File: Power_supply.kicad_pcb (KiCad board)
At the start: 2 copper layers, 116 x 60 mm, 44 parts, among them J1 Transformers, J2 240V, J20 HV_Transformer, J21 LV_Transformer, J22 220V, J23 Transformers, J25 Anodes_enable, J3 6V3, Q1 STP4NK60ZFP(MJE13003), Q10 MPSA42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

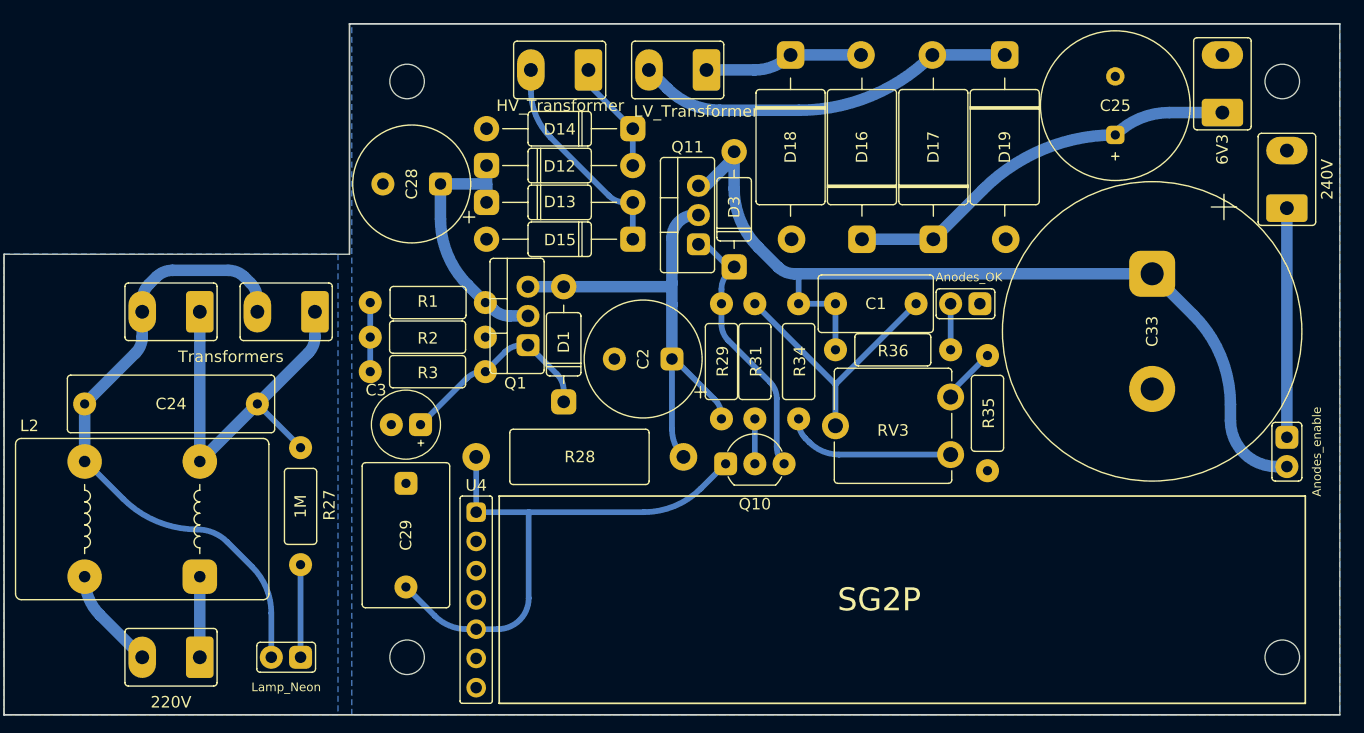
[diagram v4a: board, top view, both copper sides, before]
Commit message: Teardrops
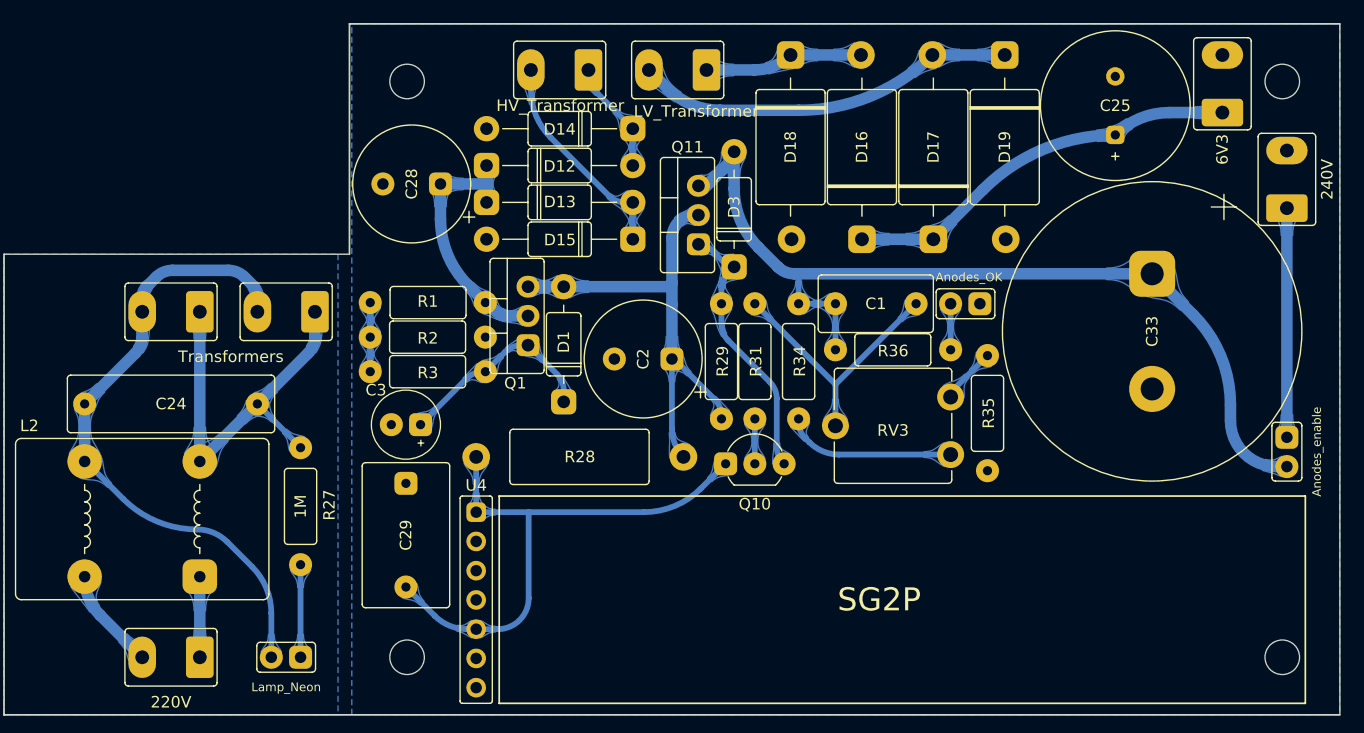
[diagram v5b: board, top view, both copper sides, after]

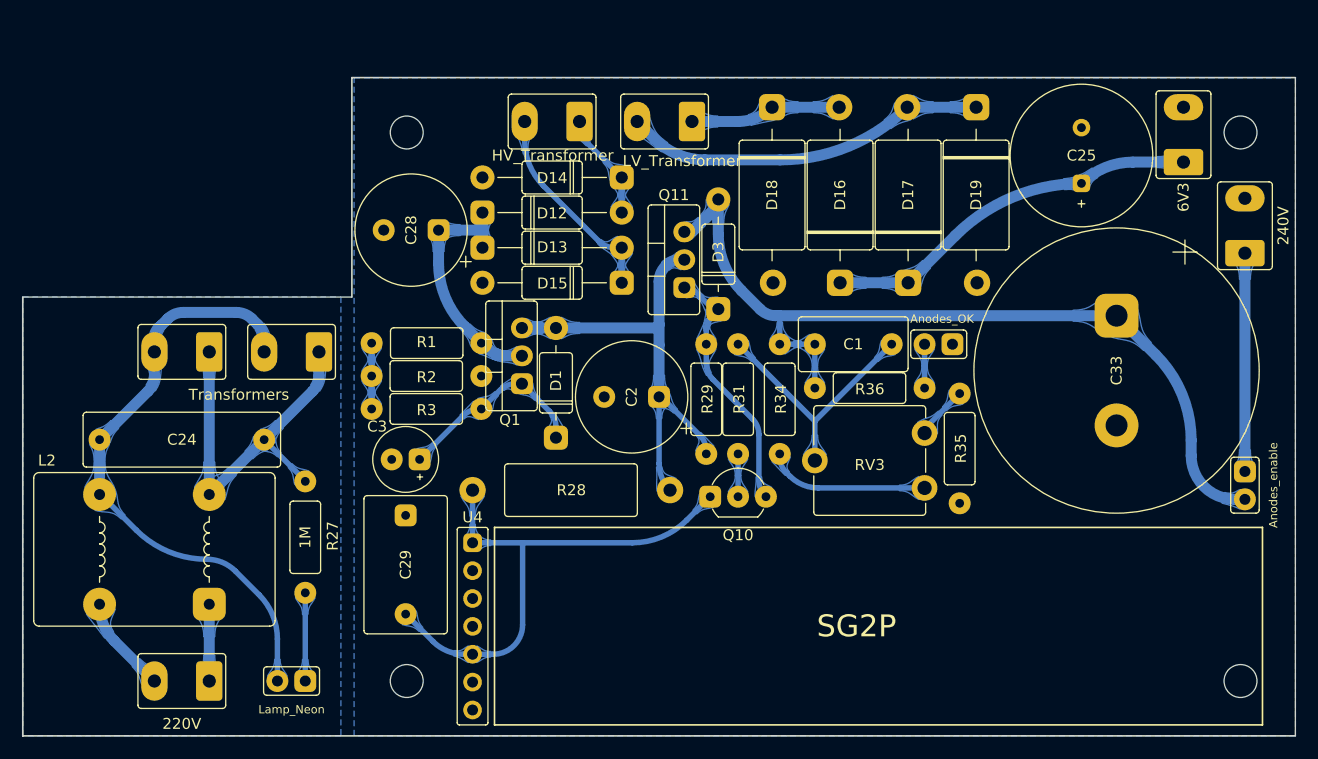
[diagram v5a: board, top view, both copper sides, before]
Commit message: Power supply PCB updated
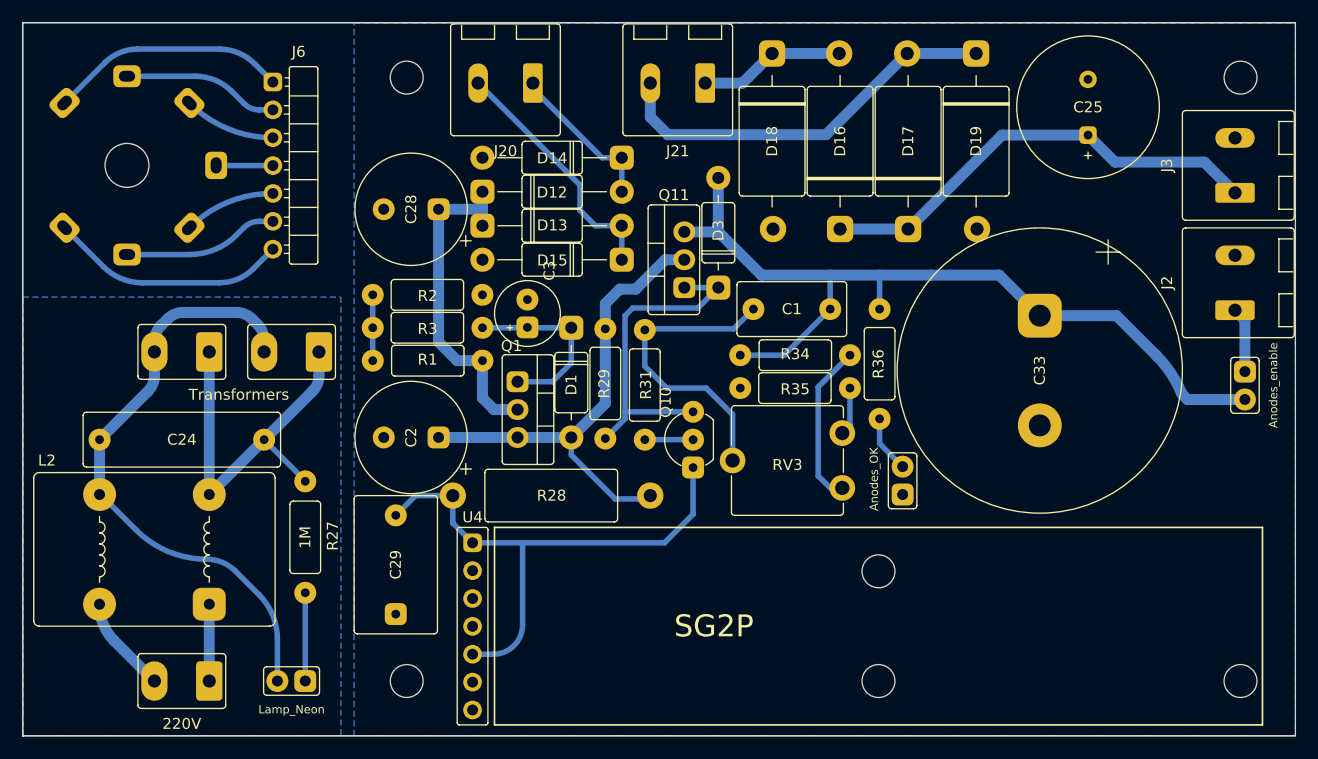
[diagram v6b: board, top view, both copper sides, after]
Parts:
- added J6: Conn_01x07, spdf1626_lib:PinHeader_1x07_P2.54mm_Horizontal, F.Cu at (84.8, 90.4)
- added U3: 6H2P, spdf1626_lib:7-pin_tube_socket, B.Cu at (71.5, 98.0)
- J2, J20, J21, J3: footprint spdf1626_lib:Connector_1x02_P5mm_Vertical -> spdf1626_lib:MCV_1,5_4-G-5.0_1x02_P5.0mm_Vertical
- moved C2 20.4 mm to (97.4, 122.8)
- moved C3 17.3 mm to (108.0, 111.5), turned to 90 degrees
- moved R35 16.0 mm to (132.4, 118.3), turned to 180 degrees
- moved NE4 14.4 mm to (142.2, 128.0), turned to 180 degrees
- moved R29 9.31 mm to (115.1, 117.9), turned to 90 degrees
- moved J25 9.10 mm to (173.4, 116.8)
- moved R31 8.60 mm to (118.7, 118.0)
- moved RV3 7.50 mm to (136.7, 122.4)
- moved R2 7.40 mm to (98.9, 109.8)
- moved R3 7.40 mm to (98.9, 112.8)
- moved C33 7.00 mm to (154.7, 116.7)
- moved Q10 6.62 mm to (123.1, 123.0), turned to 90 degrees
- moved C1 6.45 mm to (132.1, 111.1), turned to 0 degrees
- moved J20 5.51 mm to (106.0, 90.5)
- moved J3 5.47 mm to (172.5, 98.0)
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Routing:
- net (no net): track 0.00 -> 94.1 mm
- net 240V: track 19.9 -> 5.97 mm
- net Net-(D3-Pad1): track 23.3 -> 31.5 mm
- net HV: track 24.5 -> 32.4 mm
- net +6V: track 34.8 -> 41.7 mm
- net Net-(C1-Pad1): track 23.4 -> 28.0 mm
- net Net-(D12-Pad2): track 9.89 -> 14.3 mm
- net Net-(D13-Pad2): track 18.9 -> 22.9 mm
- net Net-(D17-Pad2): track 33.2 -> 36.5 mm
- net Net-(C2-Pad1): track 42.2 -> 45.0 mm
- net Net-(C1-Pad2): track 80.4 -> 78.9 mm
- net Net-(NE4-Pad2): track 4.00 -> 5.23 mm
- net Net-(C3-Pad1): track 18.1 -> 16.9 mm
- net Net-(C29-Pad2): track 48.8 -> 49.9 mm
- net Net-(R35-Pad1): track 4.93 -> 4.39 mm
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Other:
- board size 116 x 60 mm -> 116 x 65 mm

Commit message: Rounded corners for power supply PCB
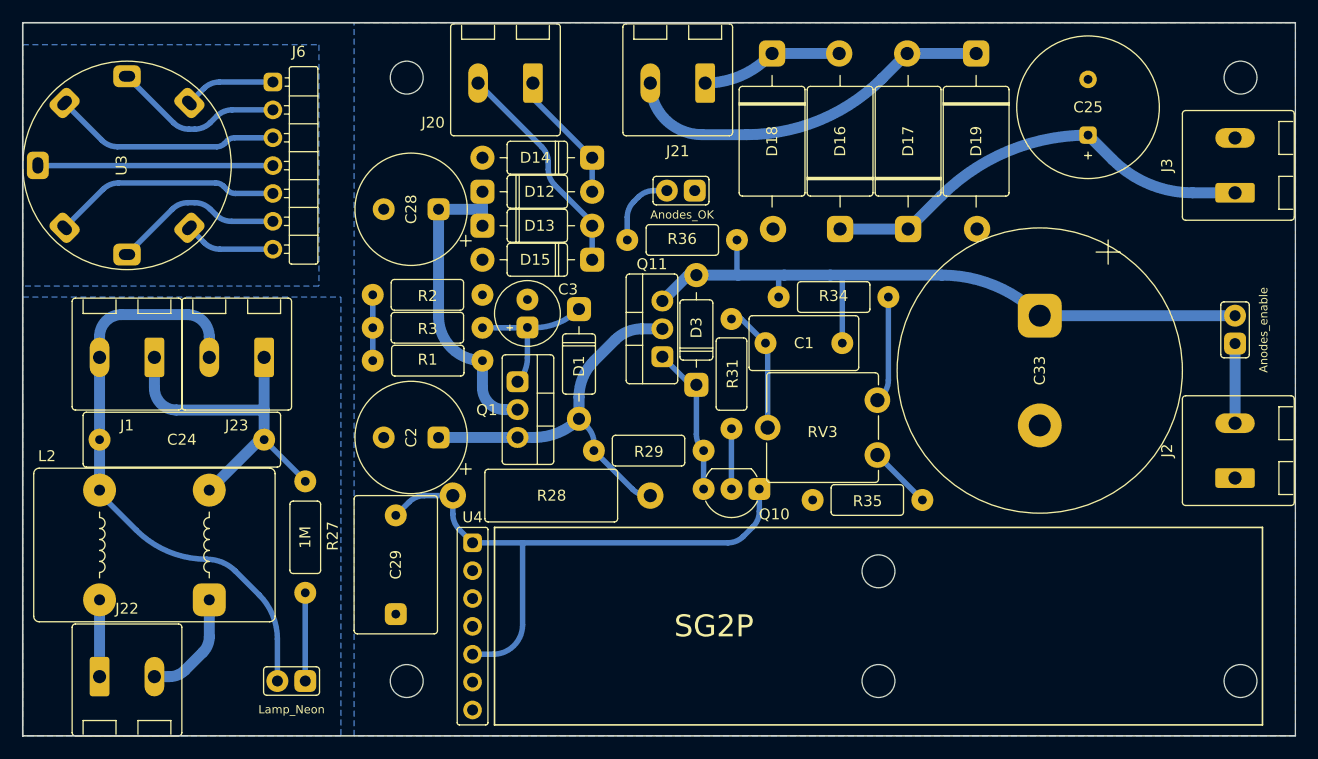
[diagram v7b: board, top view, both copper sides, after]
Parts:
- D12, D13, D14, D15: footprint spdf1626_lib:D_DO-41 -> spdf1626_lib:D_DO-41_short
- J1, J22, J23: footprint spdf1626_lib:Connector_1x02_P5mm_Vertical -> spdf1626_lib:MCV_1,5_4-G-5.0_1x02_P5.0mm_Vertical
- U3: moved to F.Cu
- moved NE4 33.6 mm to (123.2, 100.3), turned to -90 degrees
- moved R36 21.3 mm to (122.1, 104.8), turned to 0 degrees
- moved J2 15.3 mm to (172.5, 124.0)
- moved R35 12.1 mm to (139.0, 128.5)
- moved D3 9.08 mm to (123.4, 113.0)
- moved R31 7.96 mm to (126.6, 117.0)
- moved D14 7.70 mm to (108.9, 97.3)
- moved D15 7.70 mm to (108.9, 106.6)
- moved R29 7.27 mm to (119.1, 124.0), turned to 180 degrees
- moved Q11 6.61 mm to (120.3, 112.9)
- moved R34 6.35 mm to (135.9, 110.0)
- moved Q10 5.70 mm to (126.6, 127.5), turned to 180 degrees
- moved J1 5.02 mm to (71.5, 115.5)
- moved J23 5.02 mm to (81.5, 115.5)
- moved J22 5.02 mm to (71.5, 144.6), turned to 0 degrees
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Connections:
- J2 pad 1: 240V -> GND
- J2 pad 2: GND -> 240V
- J22 pad 1: Net-(J22-Pad1) -> Net-(J22-Pin_1)
- J22 pad 2: Net-(J22-Pad2) -> Net-(J22-Pin_2)
- L2 pad 1: Net-(J22-Pad1) -> Net-(J22-Pin_2)
- L2 pad 4: Net-(J22-Pad2) -> Net-(J22-Pin_1)
- RV3 pad 1: Net-(R35-Pad1) -> Net-(R34-Pad2)
- RV3 pad 3: Net-(R34-Pad2) -> Net-(R35-Pad1)
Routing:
- net Net-(D3-K): track 31.5 -> 13.8 mm
- net (no net): track 94.1 -> 111.2 mm
- net Net-(C1-Pad1): track 28.0 -> 11.8 mm
- net Net-(D3-A): track 78.9 -> 65.5 mm
- net Net-(J22-Pin_2): track 0.00 -> 10.2 mm
- net Net-(J22-Pad2): track 8.85 -> 0.00 mm
- net Net-(D1-A): track 45.0 -> 36.2 mm
- net Net-(J22-Pin_1): track 0.00 -> 7.00 mm
- net Net-(J22-Pad1): track 7.00 -> 0.00 mm
- net Net-(R34-Pad2): track 14.9 -> 9.72 mm
- net Net-(Q10-E): track 49.9 -> 53.9 mm
- net Net-(D13-A): track 22.9 -> 20.2 mm
- net Net-(D1-K): track 16.9 -> 14.4 mm
- net Net-(D12-A): track 14.3 -> 12.1 mm
- net Net-(D17-A): track 36.5 -> 34.4 mm
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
